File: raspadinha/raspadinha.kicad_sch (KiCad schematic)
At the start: 9 parts, among them J1 ATX-24, M1 Fan_CPU_4pin, Q1 IRF640N

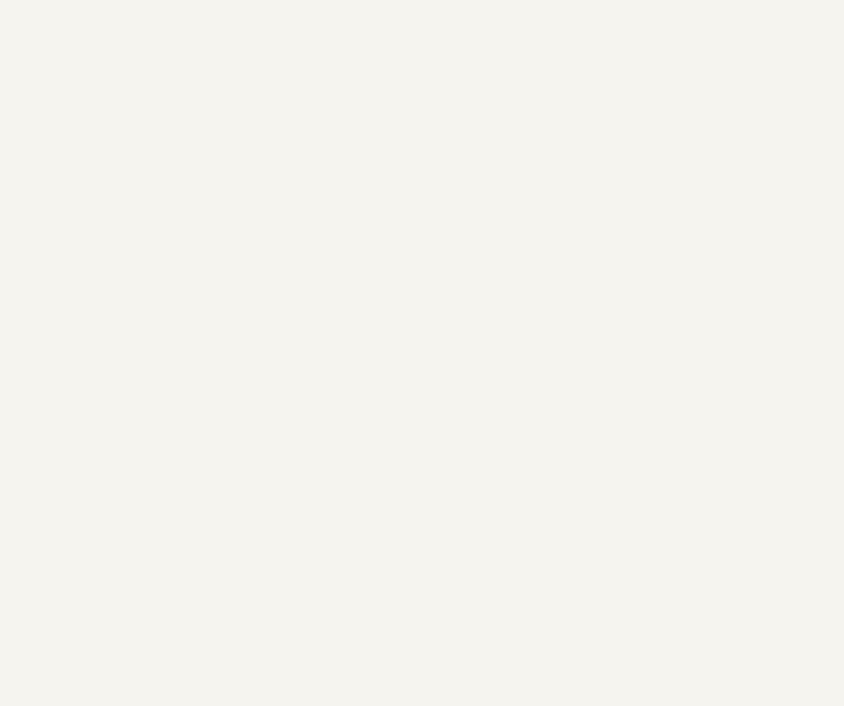
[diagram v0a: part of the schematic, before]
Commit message: feat: Circuito de controle do Motor
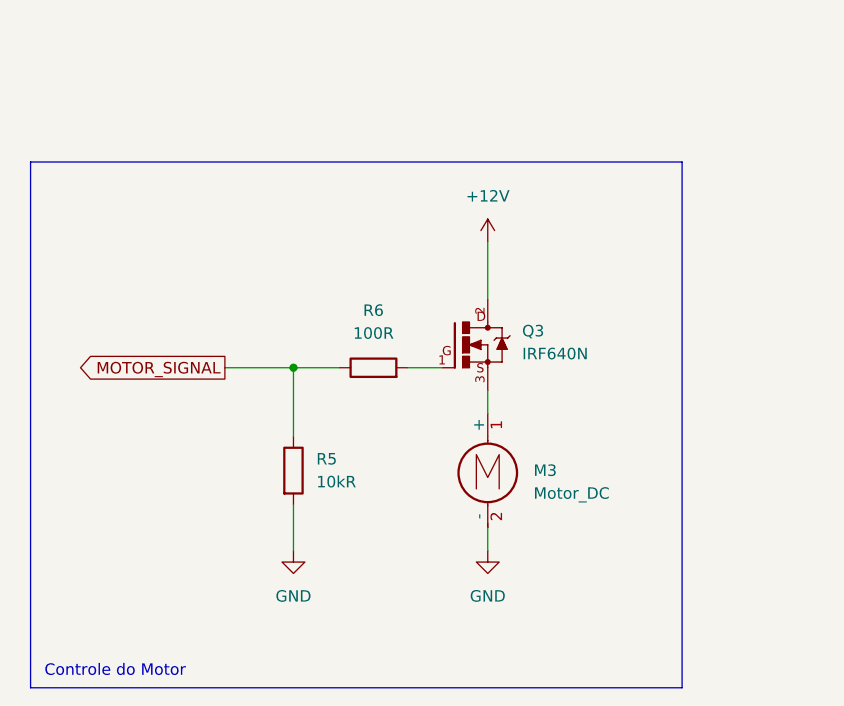
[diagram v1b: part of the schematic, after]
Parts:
- added M3: Motor_DC, symbol Motor:Motor_DC
- added Q3: IRF640N, symbol IRF640N:IRF640N
- added R5: 10kR, symbol Device:R
- added R6: 100R, symbol Device:R
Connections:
- net +12V: now also Q3.2
- net GND: now also M3.2 (-), R5.2
- new net: M3.1 (+), Q3.3
- new net: Q3.1, R6.2
- new net MOTOR_SIGNAL: R5.1, R6.1
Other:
- note added: "Controle do Motor"

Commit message: feat: Eletrônica da interface
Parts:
- added BZ1: Buzzer, symbol Device:Buzzer
- added D1: 1N4002, Diode_THT:D_DO-41_SOD81_P10.16mm_Horizontal, symbol Diode:1N4002
- added DS1: ~, symbol Sorvete:Display_LCD_16x2_I2C
- added Q2: BC338, symbol Transistor_BJT:BC338
- added R10: 100R, symbol Device:R
- added R11, R12, R13, R7, R8, R9: 10kR, symbol Device:R
- added SW1: RotaryEncoder_Switch, symbol Device:RotaryEncoder_Switch
- J1: footprint Connector_Molex:Molex_Mini-Fit_Jr_5566-24A_2x12_P4.20mm_Vertical -> (none)
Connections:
- net +3.3V: now also R11.1, R13.1, SW1.S1
- net +5V: now also BZ1.1 (+), DS1.2 (VCC), R7.1, R8.1
- net GND: now also D1.2 (A), DS1.1 (GND), Q2.3 (E), R12.2, R9.2, SW1.C
- net at M3.1 (+), Q3.3: now also D1.1 (K)
- new net: Q2.2 (B), R10.2
- new net: BZ1.2 (-), Q2.1 (C)
- new net BUZZER_SIGNAL: R10.1, R9.1
- new net DISPLAY_SCL_SIGNAL: DS1.4 (SCL), R7.2
- new net DISPLAY_SDA_SIGNAL: DS1.3 (SDA), R8.2
- new net ROTARY_SIGNAL_A: R11.2, SW1.A
- new net ROTARY_SIGNAL_B: R13.2, SW1.B
- new net ROTARY_SIGNAL_SWITCH: R12.1, SW1.S2
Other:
- note added: "Interface"
- moved on the sheet: M3, Q3

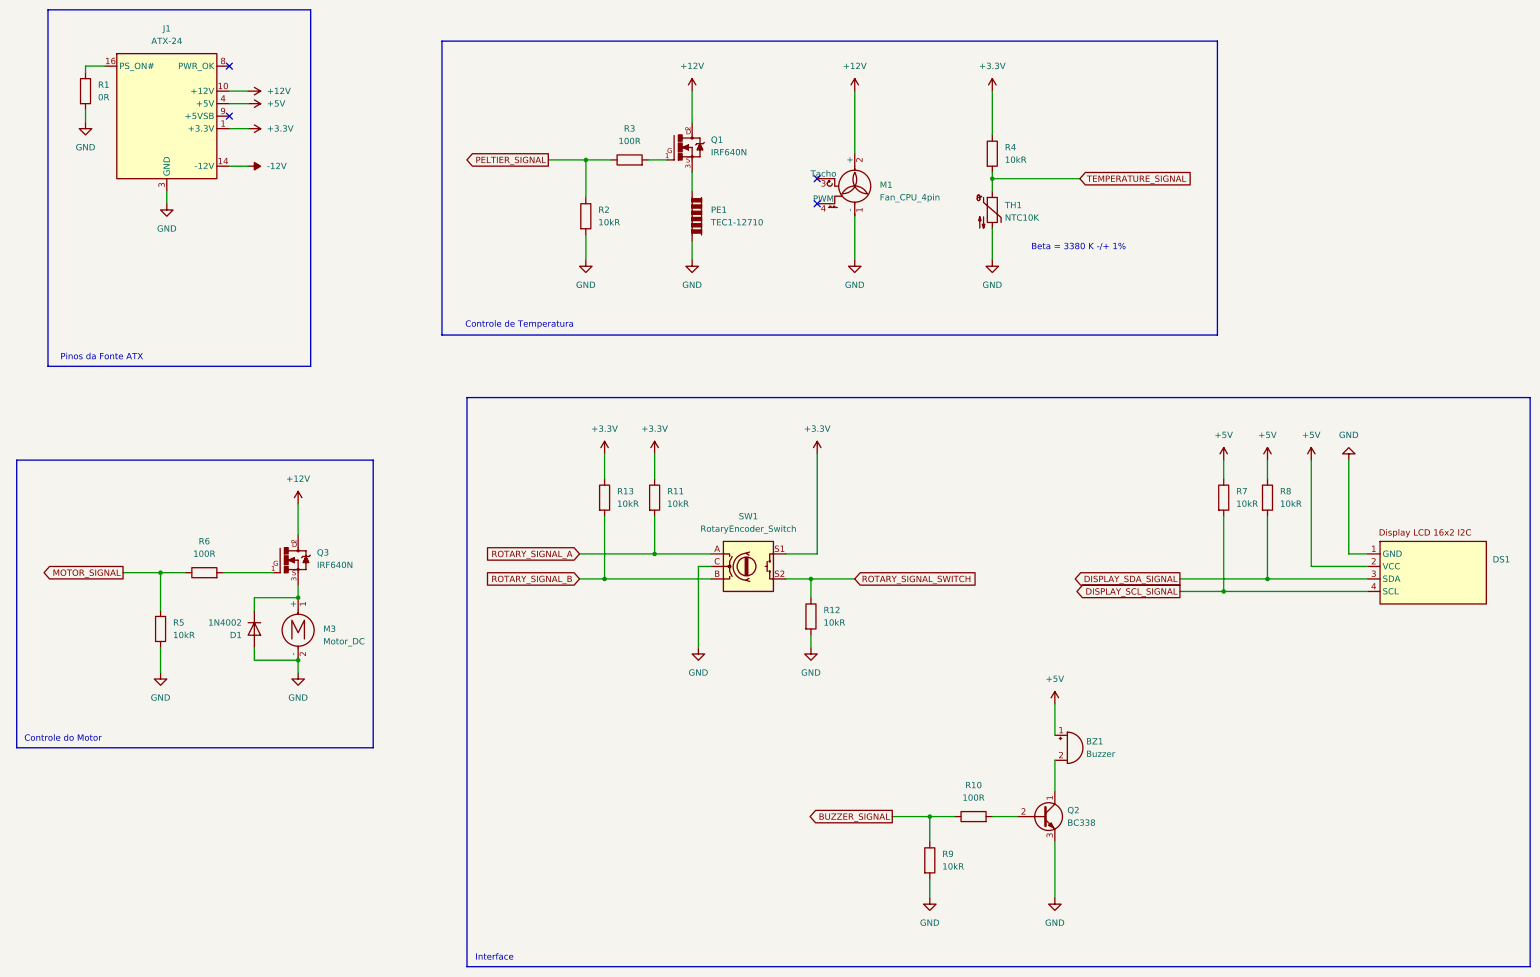
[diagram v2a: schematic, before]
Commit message: feat: Modularização do esquema elétrico
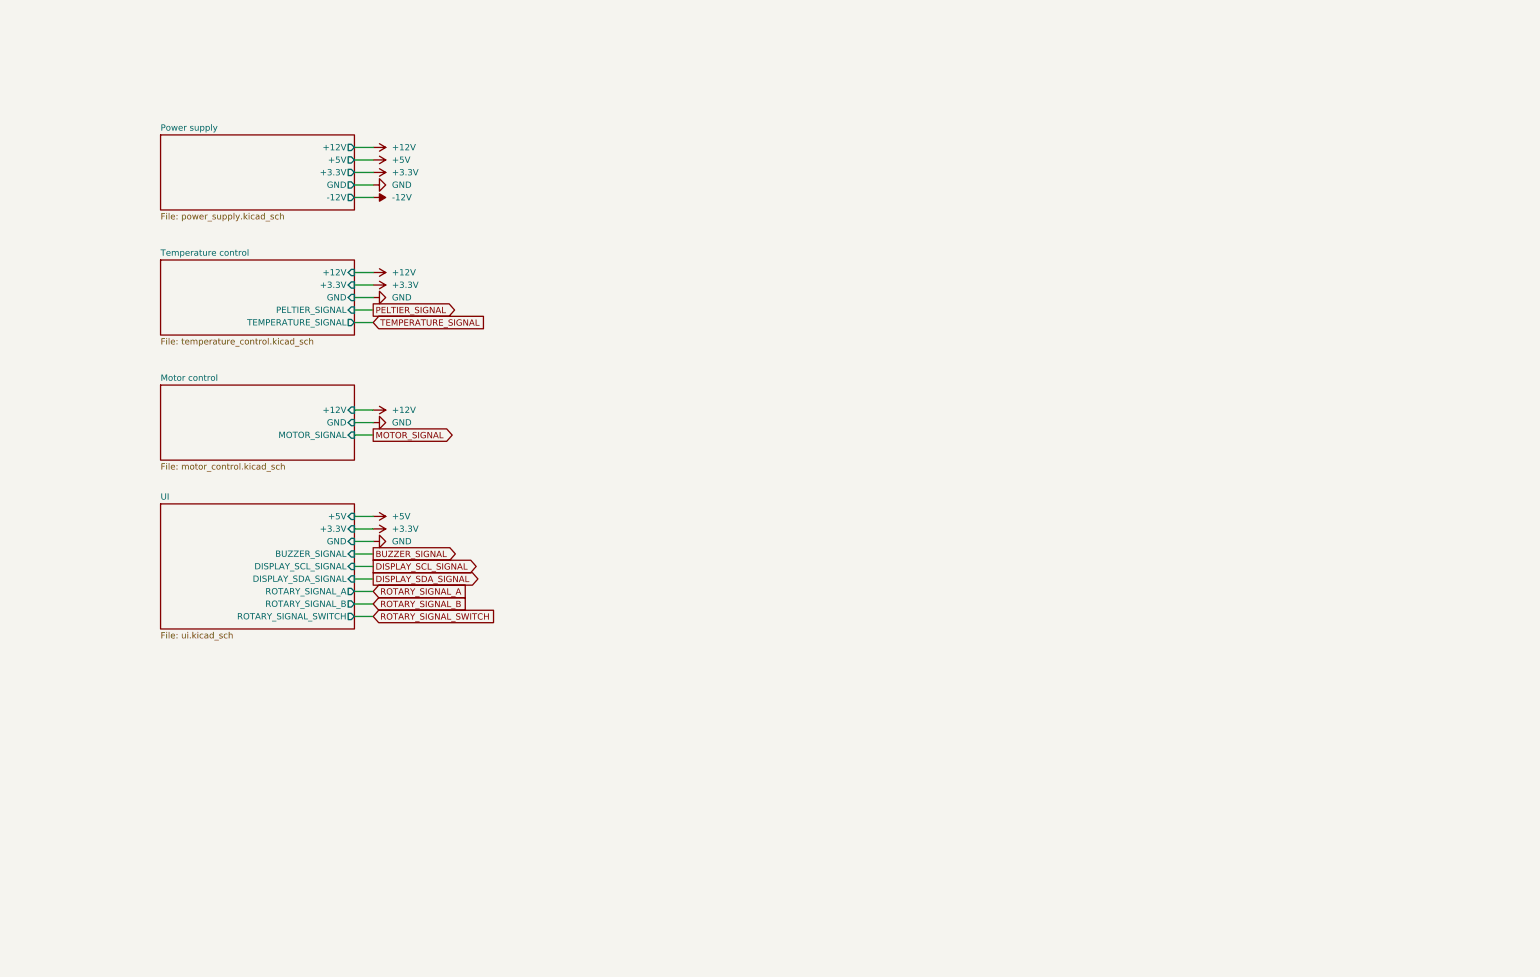
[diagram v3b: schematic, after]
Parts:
- removed BZ1: Buzzer, symbol Device:Buzzer
- removed D1: 1N4002, Diode_THT:D_DO-41_SOD81_P10.16mm_Horizontal, symbol Diode:1N4002
- removed DS1: ~, symbol Sorvete:Display_LCD_16x2_I2C
- removed J1: ATX-24, symbol Connector:ATX-24
- removed M1: Fan_CPU_4pin, symbol Motor:Fan_CPU_4pin
- removed M3: Motor_DC, symbol Motor:Motor_DC
- removed PE1: TEC1-12710, symbol Device:PeltierElement
- removed Q1, Q3: IRF640N, symbol IRF640N:IRF640N
- removed Q2: BC338, symbol Transistor_BJT:BC338
- removed R1: 0R, symbol Device:R
- removed R10, R3, R6: 100R, symbol Device:R
- removed R11, R12, R13, R2, R4, R5, R7, R8, R9: 10kR, symbol Device:R
- removed SW1: RotaryEncoder_Switch, symbol Device:RotaryEncoder_Switch
- removed TH1: NTC10K, symbol Device:Thermistor_NTC
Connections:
- no-connect marks 4 -> 0
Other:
- added sheet Motor control (motor_control.kicad_sch)
- added sheet Power supply (power_supply.kicad_sch)
- added sheet Temperature control (temperature_control.kicad_sch)
- added sheet UI (ui.kicad_sch)
- note removed: "Beta = 3380 K -/+ 1%"
- note removed: "Controle de Temperatura"
- note removed: "Controle do Motor"
- note removed: "Interface"
- note removed: "Pinos da Fonte ATX"

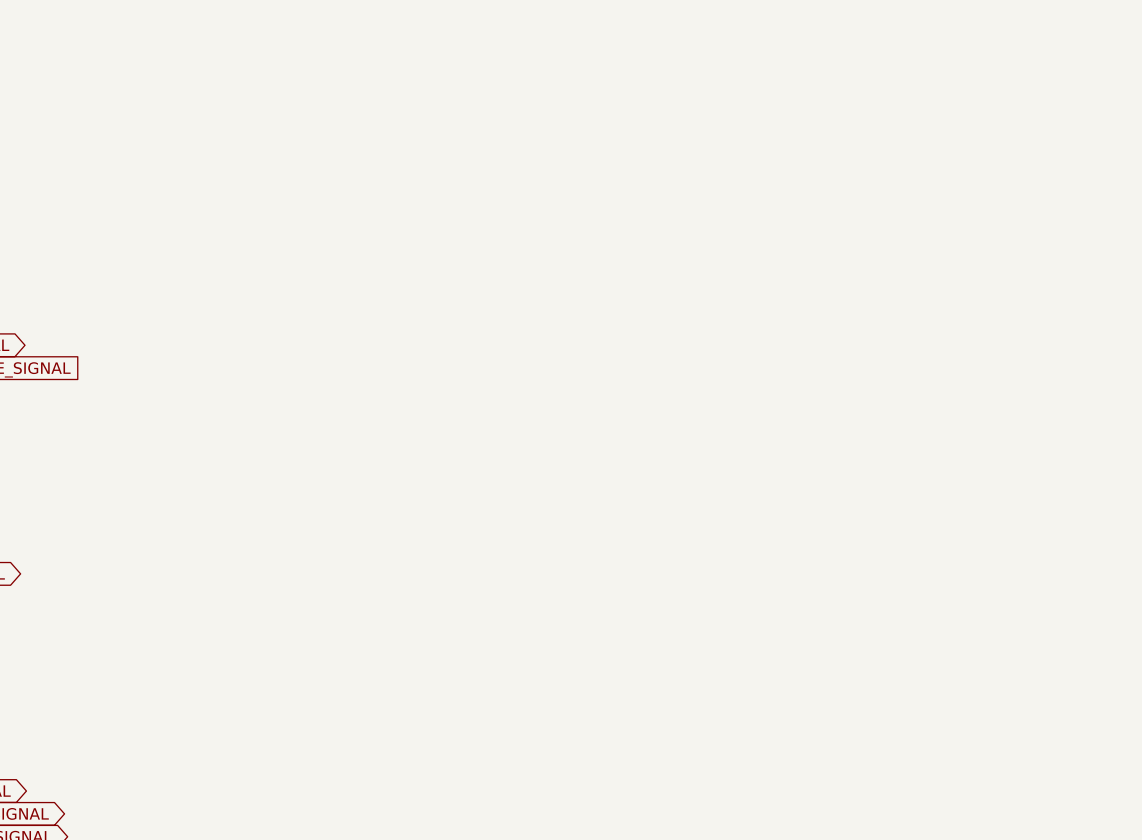
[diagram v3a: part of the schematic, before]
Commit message: feat: Conexões da ESP32
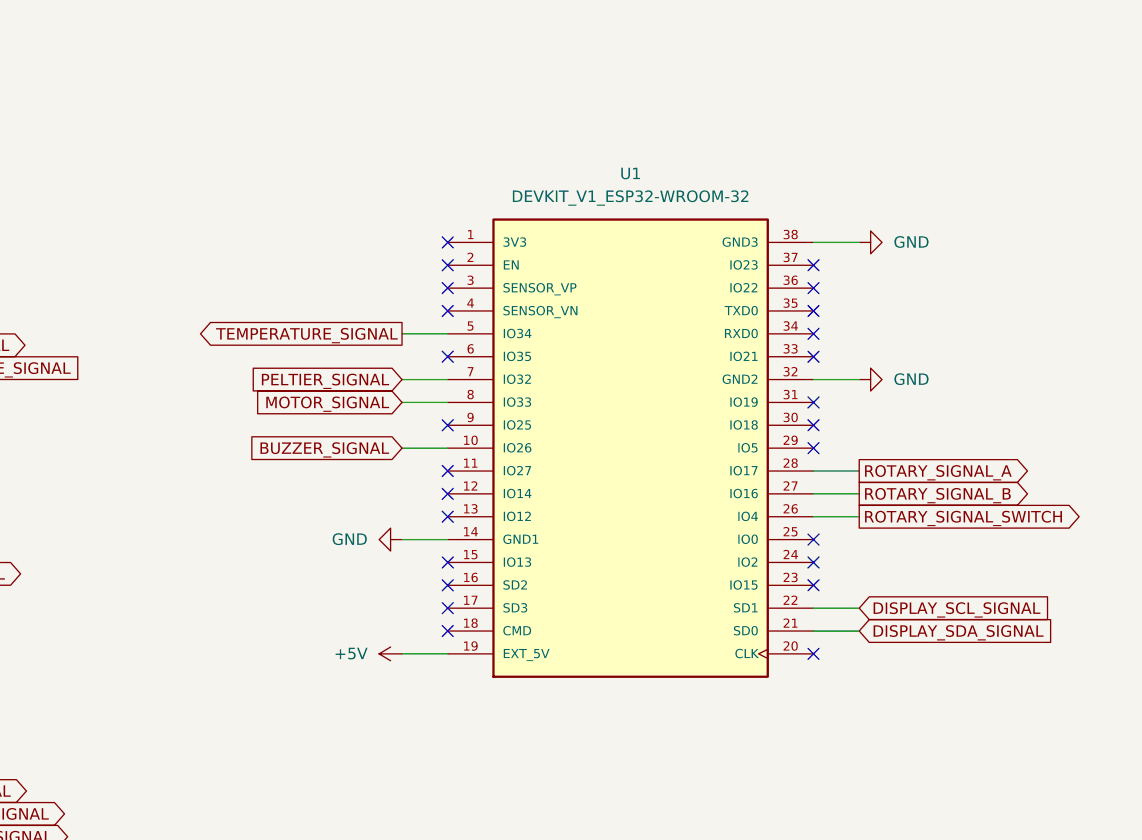
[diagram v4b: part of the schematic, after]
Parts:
- added U1: DEVKIT_V1_ESP32-WROOM-32, DEVKIT_V1_ESP32-WROOM-32:MODULE_DEVKIT_V1_ESP32-WROOM-32, symbol DEVKIT_V1_ESP32-WROOM-32:DEVKIT_V1_ESP32-WROOM-32
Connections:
- net +5V: now also U1.19 (EXT_5V)
- net BUZZER_SIGNAL: now also U1.10 (IO26)
- net DISPLAY_SCL_SIGNAL: now also U1.22 (SD1)
- net DISPLAY_SDA_SIGNAL: now also U1.21 (SD0)
- net GND: now also U1.14 (GND1), U1.32 (GND2), U1.38 (GND3)
- net MOTOR_SIGNAL: now also U1.8 (IO33)
- net PELTIER_SIGNAL: now also U1.7 (IO32)
- net ROTARY_SIGNAL_A: now also U1.28 (IO17)
- net ROTARY_SIGNAL_B: now also U1.27 (IO16)
- net ROTARY_SIGNAL_SWITCH: now also U1.26 (IO4)
- net TEMPERATURE_SIGNAL: now also U1.5 (IO34)
- no-connect marks 0 -> 25

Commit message: feat: Os Footprint foram todos atribuidos fix: A placa da Esp32 foi trocada pela que temos disponível
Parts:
- removed U1: DEVKIT_V1_ESP32-WROOM-32, DEVKIT_V1_ESP32-WROOM-32:MODULE_DEVKIT_V1_ESP32-WROOM-32, symbol DEVKIT_V1_ESP32-WROOM-32:DEVKIT_V1_ESP32-WROOM-32
- added U1: ESP32-DEVKIT-V1, ESP32-DEVKIT-V1:MODULE_ESP32_DEVKIT_V1, symbol ESP32-DEVKIT-V1:ESP32-DEVKIT-V1
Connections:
- net +5V: now also U1.30 (VIN)
- net BUZZER_SIGNAL: now also U1.9 (D18)
- net DISPLAY_SCL_SIGNAL: now also U1.14 (D22)
- net DISPLAY_SDA_SIGNAL: now also U1.11 (D21)
- net GND: now also U1.2 (GND), U1.29 (GND)
- net MOTOR_SIGNAL: now also U1.22 (D33)
- net PELTIER_SIGNAL: now also U1.21 (D32)
- net ROTARY_SIGNAL_A: now also U1.23 (D25)
- net ROTARY_SIGNAL_B: now also U1.24 (D26)
- net ROTARY_SIGNAL_SWITCH: now also U1.25 (D27)
- net TEMPERATURE_SIGNAL: now also U1.19 (D34)
- no-connect marks 25 -> 19

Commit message: feat: Refatoração da alimentação da placa feat: Renomeação do número dos componentes
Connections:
- no-connect marks 19 -> 18
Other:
- sheet Power supply ports: added none; removed -12V
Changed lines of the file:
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@@
-	)
-	(no_connect
-		(at 96.52 57.15)
 	)
 	(no_connect
@@
 		(pts
 			(xy 195.58 99.06) (xy 200.66 99.06)
-		)
-		(stroke
-			(width 0)
-			(type default)
-		)
-	)
-	(wire
-		(pts
-			(xy 92.71 57.15) (xy 96.52 57.15)
 		)
 		(stroke
@@
 		(dnp no)
 		(fields_autoplaced yes)
-		(property "Reference" "#PWR011"
+		(property "Reference" "#PWR012"
 			(at 102.87 127 0)
 			(effects
@@
 			(project "raspadinha"
 				(path "/0ce4bf39-76b0-428c-8682-47e2500753cc"
-					(reference "#PWR011")
+					(reference "#PWR012")
 					(unit 1)
 				)
@@
 		(dnp no)
 		(fields_autoplaced yes)
-		(property "Reference" "#PWR013"
+		(property "Reference" "#PWR011"
 			(at 92.71 124.46 0)
 			(effects
@@
 			(project "raspadinha"
 				(path "/0ce4bf39-76b0-428c-8682-47e2500753cc"
-					(reference "#PWR013")
+					(reference "#PWR011")
 					(unit 1)
 				)
@@
 		(dnp no)
 		(fields_autoplaced yes)
-		(property "Reference" "#PWR014"
+		(property "Reference" "#PWR013"
 			(at 163.83 63.5 0)
 			(effects
@@
 			(project ""
 				(path "/0ce4bf39-76b0-428c-8682-47e2500753cc"
-					(reference "#PWR014")
+					(reference "#PWR013")
 					(unit 1)
 				)
@@
 		(dnp no)
 		(fields_autoplaced yes)
-		(property "Reference" "#PWR09"
+		(property "Reference" "#PWR08"
 			(at 92.71 100.33 0)
 			(effects
@@
 			(project "raspadinha"
 				(path "/0ce4bf39-76b0-428c-8682-47e2500753cc"
-					(reference "#PWR09")
+					(reference "#PWR08")
 					(unit 1)
 				)
@@
 		(dnp no)
 		(fields_autoplaced yes)
-		(property "Reference" "#PWR07"
+		(property "Reference" "#PWR06"
 			(at 92.71 74.93 0)
 			(effects
@@
 			(project "raspadinha"
 				(path "/0ce4bf39-76b0-428c-8682-47e2500753cc"
-					(reference "#PWR07")
+					(reference "#PWR06")
 					(unit 1)
 				)
@@
 		(dnp no)
 		(fields_autoplaced yes)
-		(property "Reference" "#PWR012"
+		(property "Reference" "#PWR010"
 			(at 92.71 121.92 0)
 			(effects
@@
 			(project "raspadinha"
 				(path "/0ce4bf39-76b0-428c-8682-47e2500753cc"
-					(reference "#PWR012")
+					(reference "#PWR010")
 					(unit 1)
 				)
@@
 		(dnp no)
 		(fields_autoplaced yes)
-		(property "Reference" "#PWR010"
+		(property "Reference" "#PWR09"
 			(at 102.87 102.87 0)
 			(effects
@@
 			(project "raspadinha"
 				(path "/0ce4bf39-76b0-428c-8682-47e2500753cc"
-					(reference "#PWR010")
+					(reference "#PWR09")
 					(unit 1)
 				)
@@
 		(dnp no)
 		(fields_autoplaced yes)
-		(property "Reference" "#PWR015"
+		(property "Reference" "#PWR014"
 			(at 207.01 114.3 0)
 			(effects
@@
 			(project ""
 				(path "/0ce4bf39-76b0-428c-8682-47e2500753cc"
-					(reference "#PWR015")
+					(reference "#PWR014")
 					(unit 1)
 				)
@@
 		(dnp no)
 		(fields_autoplaced yes)
-		(property "Reference" "#PWR06"
+		(property "Reference" "#PWR05"
 			(at 92.71 72.39 0)
 			(effects
@@
 			(project "raspadinha"
 				(path "/0ce4bf39-76b0-428c-8682-47e2500753cc"
-					(reference "#PWR06")
+					(reference "#PWR05")
 					(unit 1)
 				)
@@
 		(dnp no)
 		(fields_autoplaced yes)
-		(property "Reference" "#PWR08"
+		(property "Reference" "#PWR07"
 			(at 102.87 77.47 0)
 			(effects
@@
 			(project "raspadinha"
 				(path "/0ce4bf39-76b0-428c-8682-47e2500753cc"
-					(reference "#PWR08")
+					(reference "#PWR07")
 					(unit 1)
 				)
@@
 		(dnp no)
 		(fields_autoplaced yes)
-		(property "Reference" "#PWR05"
+		(property "Reference" "#PWR04"
 			(at 102.87 54.61 0)
 			(effects
@@
 			(project ""
 				(path "/0ce4bf39-76b0-428c-8682-47e2500753cc"
-					(reference "#PWR05")
+					(reference "#PWR04")
 					(unit 1)
 				)
@@
 			(effects
 				(font
-					(size 1.27 1.27)
-				)
-				(justify right)
-			)
-		)
-		(pin "-12V" output
-			(at 92.71 57.15 0)
-			(effects
-				(font
